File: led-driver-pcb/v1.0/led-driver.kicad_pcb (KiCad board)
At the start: 2 copper layers, 37 x 48 mm, 38 parts, among them M3A P***, M3B P***, M3C P***, M3D P***, P1 POWER, P2 CTRL, P3 LED, Q1 MOSFET_N, Q2 MOSFET_N, U1 MAX16834

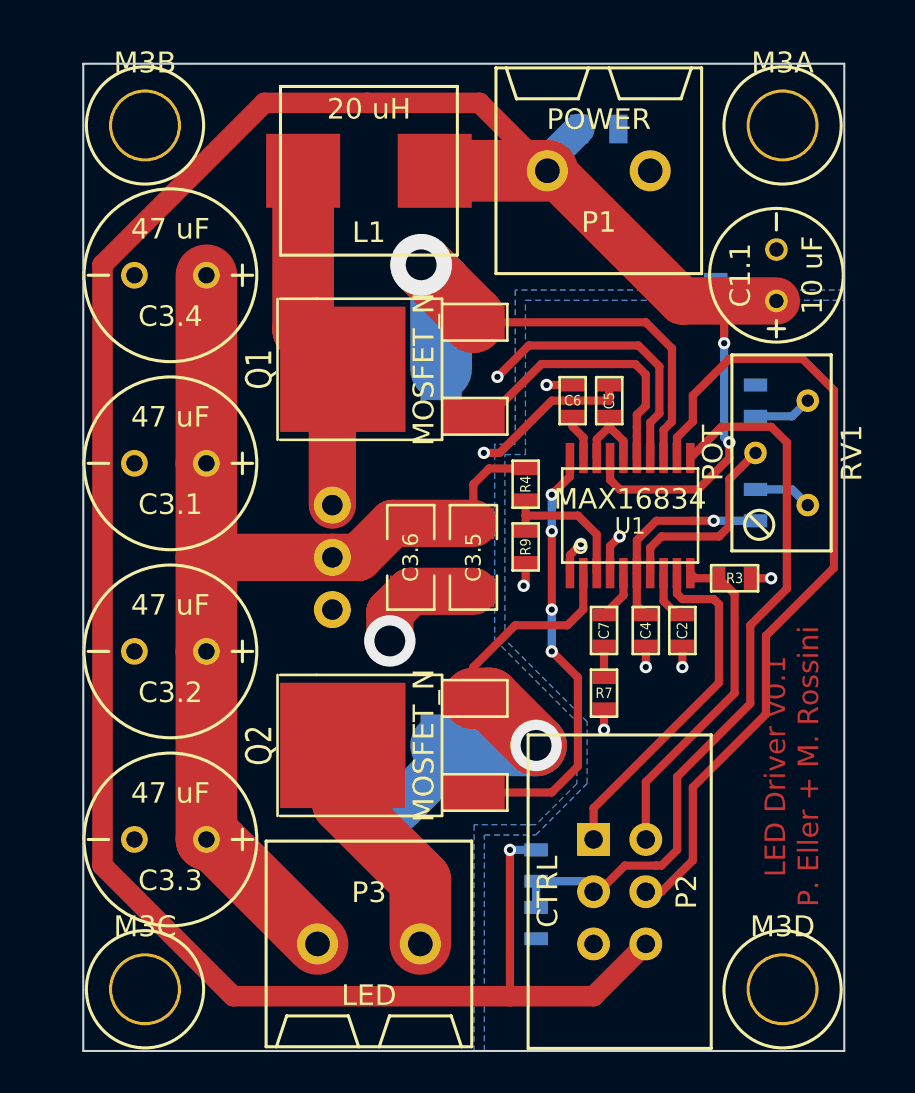
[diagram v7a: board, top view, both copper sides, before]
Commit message: Exchanged capacitors and added new ones to allow for current ripple and to minimize ESR.
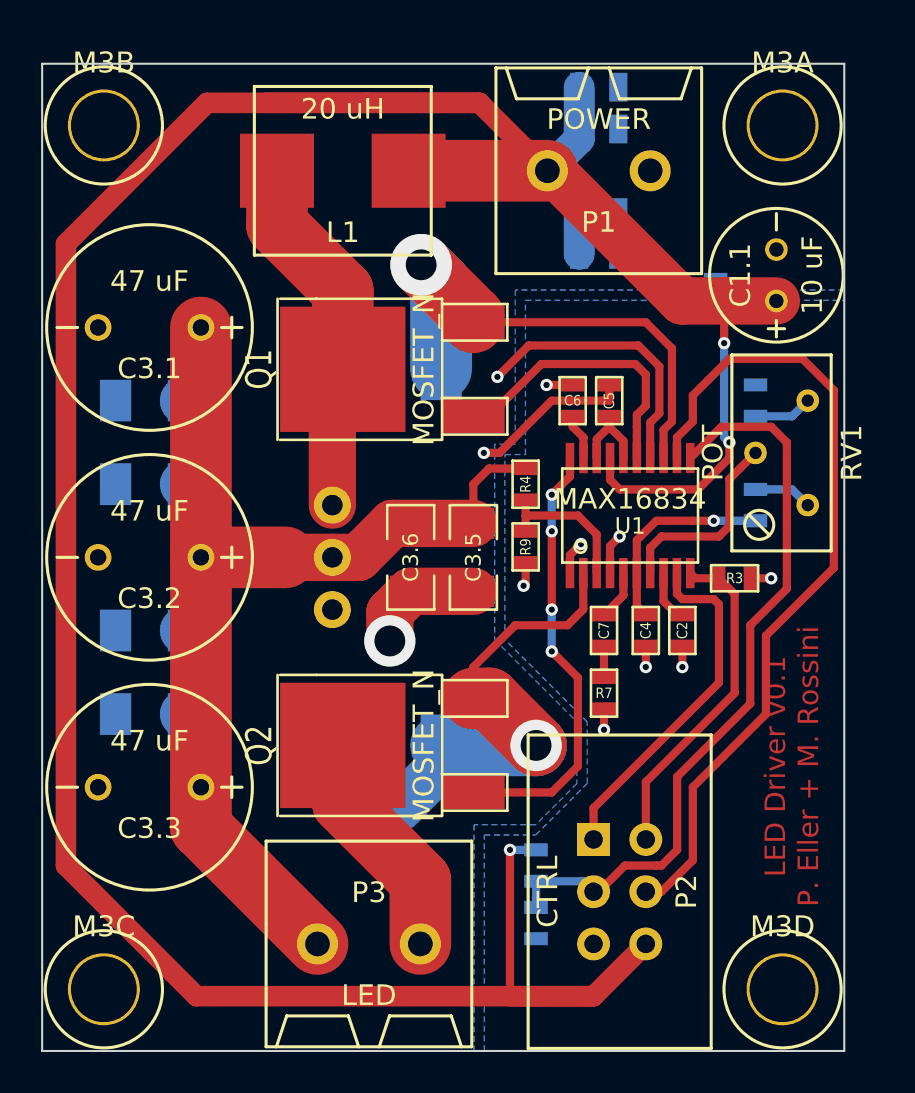
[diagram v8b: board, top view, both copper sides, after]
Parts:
- added C1.3: 1 uF, SM0805, B.Cu at (204.1, 129.2)
- added C1.4: 1 uF, SM0805, B.Cu at (204.1, 133.2)
- added C1.5: 1 uF, SM0805, B.Cu at (204.1, 135.3)
- added C3.7: 1 uF, SM1206, B.Cu at (182.2, 146.4)
- added C3.8: 1 uF, SM1206, B.Cu at (182.2, 153.6)
- added C3.9: 1 uF, SM1206, B.Cu at (182.2, 157.6)
- C3.1, C3.2, C3.3: footprint CP8x3.5 -> CP10x5
- C3.4: value 47 uF -> 1 uF; footprint CP8x3.5 -> SM1206; moved to B.Cu
- moved C3.1 6.68 mm to (182.2, 138.8)
- moved C3.4 6.18 mm to (182.2, 142.4), turned to 0 degrees
- moved C3.2 4.68 mm to (182.2, 150.0)
- moved C3.3 2.74 mm to (182.2, 161.2)
- moved C1.2 2.03 mm to (204.1, 127.1)
- moved M3B 2.00 mm to (180.0, 129.0)
- moved M3C 2.00 mm to (180.0, 171.0)
- moved L1 1.27 mm to (191.6, 131.2)
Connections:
- C3.1 pad 1: N-0000023 -> N-0000024
- C3.2 pad 1: N-0000023 -> N-0000024
- C3.3 pad 1: N-0000023 -> N-0000024
- C3.4 pad 1: N-0000023 -> GNDPWR
- C3.4 pad 2: GNDPWR -> N-0000024
- C3.5 pad 2: N-0000023 -> N-0000024
- C3.6 pad 2: N-0000023 -> N-0000024
- D1 pad 2: N-0000023 -> N-0000024
- P3 pad 1: N-0000023 -> N-0000024
- R4 pad 1: N-0000023 -> N-0000024
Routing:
- net N-0000024: track 0.00 -> 70.5 mm
- net N-0000023: track 53.4 -> 0.00 mm
- net N-0000021: track 185.6 -> 162.9 mm
- net N-0000019: track 17.3 -> 17.8 mm
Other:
- board size 37 x 48 mm -> 39 x 48 mm
